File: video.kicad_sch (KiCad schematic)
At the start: 36 parts, among them CN10 COMPOSITE, CN9 VIDEO_DB23M, U4 DENISE, U40 74LS245, U41 74LS245, U94 74HCT14

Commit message: BOM updates
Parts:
- RP402, RP403: MFG Name (none) -> BOURNS; MFG Part Num (none) -> 4610X-102-470LF; Mouser (none) -> 652-4610X-2LF-47
- U4: MFG Name COMMODORE -> 3M; MFG Part Num (none) -> 4848-6000-CP; Mouser (none) -> 517-4848-6000-CP
- U40, U41: MFG Part Num CD74ACT245E -> SN74LS245N; Mouser (none) -> 595-SN74LS245N
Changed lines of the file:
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@@
 			)
 		)
-		(property "Mouser" ""
+		(property "Mouser" "517-4848-6000-CP "
 			(at 87.249 92.075 0)
 			(effects
@@
 			)
 		)
-		(property "MFG Name" "COMMODORE"
+		(property "MFG Name" "3M"
+			(at 87.249 92.075 0)
+			(effects
+				(font
+					(size 1.27 1.27)
+				)
+				(hide yes)
+			)
+		)
+		(property "MFG Part Num" "4848-6000-CP "
 			(at 87.249 92.075 0)
 			(effects
@@
 			)
 		)
-		(property "MFG Part Num" "CD74ACT245E"
+		(property "MFG Part Num" "SN74LS245N "
 			(at 135.382 88.265 0)
 			(effects
@@
 			)
 		)
-		(property "Mouser" ""
+		(property "Mouser" "595-SN74LS245N "
 			(at 135.382 88.265 90)
 			(effects
@@
 			)
 		)
-		(property "MFG Part Num" "CD74ACT245E"
+		(property "MFG Part Num" "SN74LS245N "
 			(at 135.382 121.285 0)
 			(effects
@@
 			)
 		)
-		(property "Mouser" ""
+		(property "Mouser" "595-SN74LS245N "
 			(at 135.382 121.285 90)
 			(effects
@@
 			)
 		)
-		(property "Mouser" ""
+		(property "Mouser" "652-4610X-2LF-47"
+			(at 335.026 110.871 90)
+			(effects
+				(font
+					(size 1.27 1.27)
+				)
+				(hide yes)
+			)
+		)
+		(property "MFG Name" "BOURNS"
+			(at 335.026 110.871 90)
+			(effects
+				(font
+					(size 1.27 1.27)
+				)
+				(hide yes)
+			)
+		)
+		(property "MFG Part Num" "4610X-102-470LF"
 			(at 335.026 110.871 90)
 			(effects
@@
 			)
 		)
-		(property "Mouser" ""
+		(property "Mouser" "652-4610X-2LF-47"
+			(at 335.026 93.091 90)
+			(effects
+				(font
+					(size 1.27 1.27)
+				)
+				(hide yes)
+			)
+		)
+		(property "MFG Name" "BOURNS"
+			(at 335.026 93.091 90)
+			(effects
+				(font
+					(size 1.27 1.27)
+				)
+				(hide yes)
+			)
+		)
+		(property "MFG Part Num" "4610X-102-470LF"
 			(at 335.026 93.091 90)
 			(effects
@@
 			)
 		)
-		(property "MFG Part Num" "CD74ACT245E"
+		(property "MFG Part Num" "SN74LS245N "
 			(at 151.13 208.28 0)
 			(effects
@@
 			)
 		)
-		(property "Mouser" ""
+		(property "Mouser" "595-SN74LS245N "
 			(at 151.13 208.28 0)
 			(effects
@@
 			)
 		)
-		(property "MFG Part Num" "CD74ACT245E"
+		(property "MFG Part Num" "SN74LS245N "
 			(at 189.23 208.28 0)
 			(effects
@@
 			)
 		)
-		(property "Mouser" ""
+		(property "Mouser" "595-SN74LS245N "
 			(at 189.23 208.28 0)
 			(effects
@@
 			)
 		)
-		(property "Mouser" ""
+		(property "Mouser" "517-4848-6000-CP "
 			(at 90.17 207.01 0)
 			(effects
@@
 			)
 		)
-		(property "MFG Name" "COMMODORE"
+		(property "MFG Name" "3M"
 			(at 90.17 207.01 0)
 			(effects
+				(font
+					(size 1.27 1.27)
+				)
+				(hide yes)
+			)
+		)
+		(property "MFG Part Num" "4848-6000-CP "
+			(at 90.17 207.01 0)
+			(effects

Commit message: even  more BOM work
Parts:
- U40, U41: value 74LS245 -> 74HCT245; MFG Part Num SN74LS245N -> (none); Mouser 595-SN74LS245N -> (none)
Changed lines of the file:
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@@
 			)
 		)
-		(property "Value" "74LS245"
+		(property "Value" "74HCT245"
 			(at 137.16 88.265 90)
 			(effects
@@
 			)
 		)
-		(property "MFG Part Num" "SN74LS245N "
+		(property "MFG Part Num" ""
 			(at 135.382 88.265 0)
 			(effects
@@
 			)
 		)
-		(property "Mouser" "595-SN74LS245N "
+		(property "Mouser" ""
 			(at 135.382 88.265 90)
 			(effects
@@
 			)
 		)
-		(property "Value" "74LS245"
+		(property "Value" "74HCT245"
 			(at 137.16 121.285 90)
 			(effects
@@
 			)
 		)
-		(property "MFG Part Num" "SN74LS245N "
+		(property "MFG Part Num" ""
 			(at 135.382 121.285 0)
 			(effects
@@
 			)
 		)
-		(property "Mouser" "595-SN74LS245N "
+		(property "Mouser" ""
 			(at 135.382 121.285 90)
 			(effects
@@
 			)
 		)
-		(property "Value" "74LS245"
+		(property "Value" "74HCT245"
 			(at 156.9212 208.788 0)
 			(effects
@@
 			)
 		)
-		(property "MFG Part Num" "SN74LS245N "
+		(property "MFG Part Num" ""
 			(at 151.13 208.28 0)
 			(effects
@@
 			)
 		)
-		(property "Mouser" "595-SN74LS245N "
+		(property "Mouser" ""
 			(at 151.13 208.28 0)
 			(effects
@@
 			)
 		)
-		(property "Value" "74LS245"
+		(property "Value" "74HCT245"
 			(at 195.0212 208.788 0)
 			(effects
@@
 			)
 		)
-		(property "MFG Part Num" "SN74LS245N "
+		(property "MFG Part Num" ""
 			(at 189.23 208.28 0)
 			(effects
@@
 			)
 		)
-		(property "Mouser" "595-SN74LS245N "
+		(property "Mouser" ""
 			(at 189.23 208.28 0)
 			(effects

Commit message: added mouser part numbers
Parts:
- U40, U41: MFG Part Num (none) -> SN74HCT245N; Mouser (none) -> 595-SN74HCT245N
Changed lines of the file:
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@@
 			)
 		)
-		(property "MFG Part Num" ""
+		(property "MFG Part Num" "SN74HCT245N "
 			(at 135.382 88.265 0)
 			(effects
@@
 			)
 		)
-		(property "Mouser" ""
+		(property "Mouser" "595-SN74HCT245N "
 			(at 135.382 88.265 90)
 			(effects
@@
 			)
 		)
-		(property "MFG Part Num" ""
+		(property "MFG Part Num" "SN74HCT245N "
 			(at 135.382 121.285 0)
 			(effects
@@
 			)
 		)
-		(property "Mouser" ""
+		(property "Mouser" "595-SN74HCT245N "
 			(at 135.382 121.285 90)
 			(effects
@@
 			)
 		)
-		(property "MFG Part Num" ""
+		(property "MFG Part Num" "SN74HCT245N "
 			(at 151.13 208.28 0)
 			(effects
@@
 			)
 		)
-		(property "Mouser" ""
+		(property "Mouser" "595-SN74HCT245N "
 			(at 151.13 208.28 0)
 			(effects
@@
 			)
 		)
-		(property "MFG Part Num" ""
+		(property "MFG Part Num" "SN74HCT245N "
 			(at 189.23 208.28 0)
 			(effects
@@
 			)
 		)
-		(property "Mouser" ""
+		(property "Mouser" "595-SN74HCT245N "
 			(at 189.23 208.28 0)
 			(effects

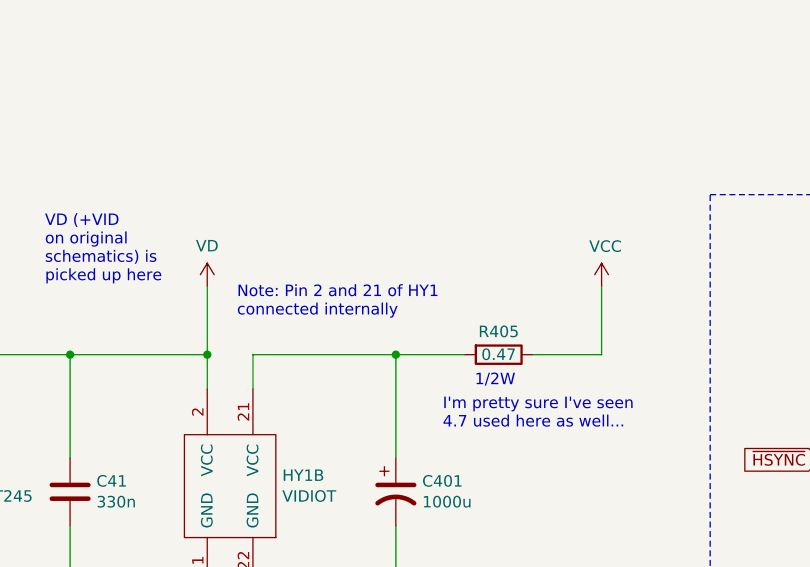
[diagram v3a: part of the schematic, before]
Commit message: replaced commodore hybrid with OpenAmigaVideoHybrid
decided to place address pullups for better EPROM capability
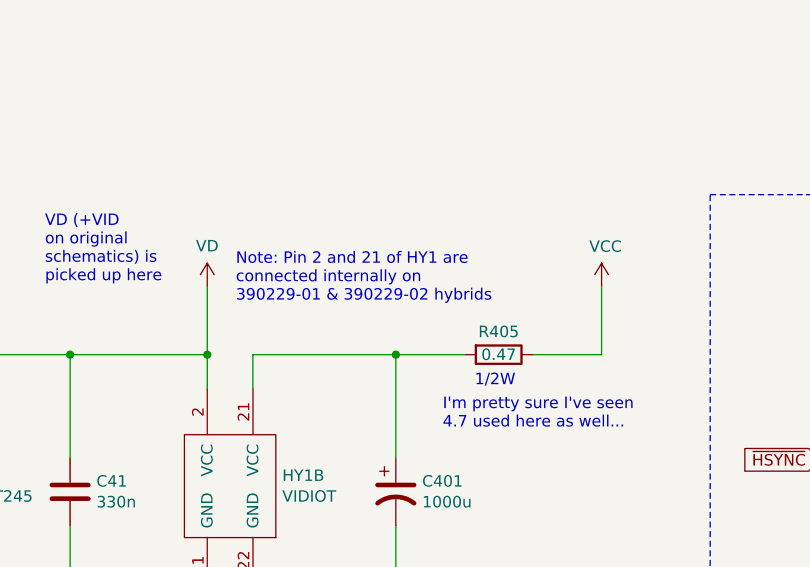
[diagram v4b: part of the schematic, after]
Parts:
- HY1: MFG Name COMMODORE -> DvW/SukkoPerra; MFG Part Num 390229-03 -> OpenAmigaVideoHybrid-04
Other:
- note added: "Note: Pin 2 and 21 of HY1 are connected internally on 390229-01 & 390229-02 hybrids"
- note removed: "Note: Pin 2 and 21 of HY1 connected internally"
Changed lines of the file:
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@@
 		)
 	)
-	(text "Note: Pin 2 and 21 of HY1\nconnected internally"
+	(text "Note: Pin 2 and 21 of HY1 are\nconnected internally on \n390229-01 & 390229-02 hybrids\n"
 		(exclude_from_sim no)
-		(at 226.822 188.976 0)
+		(at 226.695 187.325 0)
 		(effects
 			(font
@@
 			)
 		)
-		(property "MFG Name" "COMMODORE"
+		(property "MFG Name" "DvW/SukkoPerra"
 			(at 191.516 93.345 0)
 			(effects
@@
 			)
 		)
-		(property "MFG Part Num" "390229-03"
+		(property "MFG Part Num" "OpenAmigaVideoHybrid-04"
 			(at 191.516 93.345 0)
 			(effects
@@
 			)
 		)
-		(property "MFG Name" "COMMODORE"
+		(property "MFG Name" "DvW/SukkoPerra"
 			(at 226.06 208.28 0)
 			(effects
@@
 			)
 		)
-		(property "MFG Part Num" "390229-03"
+		(property "MFG Part Num" "OpenAmigaVideoHybrid-04"
 			(at 226.06 208.28 0)
 			(effects

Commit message: more silkscreen work
removed sockets for standard IC's
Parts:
- HY1: MFG Name DvW/SukkoPerra -> DVW/SUKKOPERA
- U40, U41: footprint Package_DIP:DIP-20_W7.62mm_Socket_LongPads -> Package_DIP:DIP-20_W7.62mm_LongPads
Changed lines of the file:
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@@
 	(title_block
 		(title "Rämixx500_max")
-		(date "2026-04-09")
+		(date "2026-04-26")
 		(rev "3")
 		(company "SukkoPera")
@@
 			)
 		)
-		(property "Footprint" "Package_DIP:DIP-20_W7.62mm_Socket_LongPads"
+		(property "Footprint" "Package_DIP:DIP-20_W7.62mm_LongPads"
 			(at 135.382 88.265 0)
 			(effects
@@
 			)
 		)
-		(property "Footprint" "Package_DIP:DIP-20_W7.62mm_Socket_LongPads"
+		(property "Footprint" "Package_DIP:DIP-20_W7.62mm_LongPads"
 			(at 135.382 121.285 0)
 			(effects
@@
 			)
 		)
-		(property "MFG Name" "DvW/SukkoPerra"
+		(property "MFG Name" "DVW/SUKKOPERA"
 			(at 191.516 93.345 0)
 			(effects
@@
 			)
 		)
-		(property "Footprint" "Package_DIP:DIP-20_W7.62mm_Socket_LongPads"
+		(property "Footprint" "Package_DIP:DIP-20_W7.62mm_LongPads"
 			(at 151.13 208.28 0)
 			(effects
@@
 			)
 		)
-		(property "Footprint" "Package_DIP:DIP-20_W7.62mm_Socket_LongPads"
+		(property "Footprint" "Package_DIP:DIP-20_W7.62mm_LongPads"
 			(at 189.23 208.28 0)
 			(effects
@@
 			)
 		)
-		(property "MFG Name" "DvW/SukkoPerra"
+		(property "MFG Name" "DVW/SUKKOPERA"
 			(at 226.06 208.28 0)
 			(effects

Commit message: fixed R309 wrong value
Replaced too big 2W resistors with better fitting 1W resistors
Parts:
- R405: MFG Part Num PR02000204707JA100 -> PR01000104707JA500; Mouser 594-PR02000204707JA1 -> 594-PR01000104707JA5
- R406: MFG Part Num PR02000204708JA100 -> PR01000104708JA500; Mouser 594-5083NW4R700JA100 -> 594-PR01000104708JA5
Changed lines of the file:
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@@
 			)
 		)
-		(property "Mouser" "594-5083NW4R700JA100"
+		(property "Mouser" "594-PR01000104708JA5"
 			(at 119.38 193.04 90)
 			(effects
@@
 			)
 		)
-		(property "MFG Part Num" "PR02000204708JA100 "
+		(property "MFG Part Num" "PR01000104708JA500 "
 			(at 119.38 193.04 90)
 			(effects
@@
 			)
 		)
-		(property "Mouser" "594-PR02000204707JA1 "
+		(property "Mouser" "594-PR01000104707JA5 "
 			(at 255.905 193.04 90)
 			(effects
@@
 			)
 		)
-		(property "MFG Part Num" "PR02000204707JA100"
+		(property "MFG Part Num" "PR01000104707JA500 "
 			(at 255.905 193.04 90)
 			(effects
